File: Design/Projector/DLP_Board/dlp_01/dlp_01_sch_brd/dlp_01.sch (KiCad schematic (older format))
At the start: 0 parts

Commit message: Ongoing updates the schematics
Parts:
- added C? (x2): 22u, Capacitors_SMD:C_1206, symbol Device:C
- added J?: Barrel_Jack_MountingPin, Connectors:BARREL_JACK, symbol Connector:Barrel_Jack_MountingPin
- added R?: 0R, Resistors_SMD:R_1206, symbol Device:R
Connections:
- new net: C?.1, J?.1, R?.2
- new net: C?.1, R?.1
- new net GND: C?.2, C?.2, J?.2
- no-connect marks 0 -> 1

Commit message: More updates in the DLP board
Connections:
- no-connect marks 1 -> 5
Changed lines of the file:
@@
 F64 "PDAT_A_[23..0]" I L 7700 4150 50
 F65 "3DR_A" I L 7700 4350 50
-F66 "mSPI_CLK" O L 7700 2650 50
-F67 "mSPI_MOSI" O L 7700 2700 50
-F68 "mSPI_CSZO" O L 7700 2800 50
-F69 "mSPI_MISO" I L 7700 2750 50
-F70 "mI2C_SCL" O L 7700 3650 50
-F71 "mI2C_SDA" B L 7700 3700 50
-F72 "mHOST_IRQ" O L 7700 5650 50
-F73 "CMP_OUT" I L 7700 6900 50
-F74 "LED_SEL_0" O L 7700 7100 50
-F75 "LED_SEL_1" O L 7700 7150 50
-F76 "sSPI_CLK" O L 7700 2950 50
-F77 "sSPI_MOSI" O L 7700 3000 50
-F78 "sSPI_CSZO" O L 7700 3100 50
-F79 "sSPI_MISO" I L 7700 3050 50
-F80 "sHOST_IRQ" O L 7700 5700 50
-F81 "sI2C_SCL" O L 7700 3850 50
-F82 "sI2C_SDA" B L 7700 3900 50
-F83 "PARKZ" I L 7700 5250 50
-F84 "RESETZ" I L 7700 6800 50
+F66 "mHOST_IRQ" O L 7700 5650 50
+F67 "CMP_OUT" I L 7700 6900 50
+F68 "LED_SEL_0" O L 7700 7100 50
+F69 "LED_SEL_1" O L 7700 7150 50
+F70 "sHOST_IRQ" O L 7700 5700 50
+F71 "PARKZ" I L 7700 5250 50
+F72 "RESETZ" I L 7700 6800 50
+F73 "HOST_SCL" I L 7700 3000 50
+F74 "HOST_SDA" I L 7700 3050 50
+F75 "CONTR0_SCL" I L 7700 3200 50
+F76 "CONTR0_SDA" I L 7700 3250 50
+F77 "CONTR1_SCL" I L 7700 3400 50
+F78 "CONTR1_SDA" I L 7700 3450 50
 $EndSheet
 $Sheet
@@
 F0 "application_connectors" 50
 F1 "application_connectors.sch" 50
+F2 "PCLK_B" O R 7050 4550 50
+F3 "VSYNC_B" O R 7050 4650 50
+F4 "HSYNC_B" O R 7050 4700 50
+F5 "DATEN_B" O R 7050 4750 50
+F6 "PDAT_B_[23..0]" O R 7050 4600 50
+F7 "3DR_B" O R 7050 4800 50
+F8 "PCLK_A" O R 7050 4100 50
+F9 "VSYNC_A" O R 7050 4200 50
+F10 "HSYNC_A" O R 7050 4250 50
+F11 "DATEN_A" O R 7050 4300 50
+F12 "PDAT_A_[23..0]" O R 7050 4150 50
+F13 "3DR_A" O R 7050 4350 50
+F14 "PDM_CVS_TE_B" I R 7050 4850 50
+F15 "PDM_CVS_TE_A" I R 7050 4400 50
+F16 "HOST_SCL" O R 7050 3000 50
+F17 "HOST_SDA" B R 7050 3050 50
+F18 "CONTR0_SCL" O R 7050 3200 50
+F19 "CONTR0_SDA" B R 7050 3250 50
+F20 "CONTR1_SDA" B R 7050 3450 50
+F21 "CONTR1_SCL" O R 7050 3400 50
+F22 "PS_SCL" O R 7050 2600 50
+F23 "PL_SCL" O R 7050 2650 50
+F24 "PL_SDA" B R 7050 2800 50
+F25 "PS_SDA" B R 7050 2850 50
 $EndSheet
 Wire Wire Line
@@
 Wire Wire Line
 	7050 7750 10150 7750
+Wire Wire Line
+	7050 4100 7700 4100
+Wire Wire Line
+	7050 4200 7700 4200
+Wire Bus Line
+	7050 4150 7700 4150
+Wire Wire Line
+	7050 4250 7700 4250
+Wire Wire Line
+	7050 4300 7700 4300
+Wire Wire Line
+	7050 4350 7700 4350
+Wire Wire Line
+	7050 4400 7700 4400
+Wire Wire Line
+	7050 4550 7700 4550
+Wire Bus Line
+	7050 4600 7700 4600
+Wire Wire Line
+	7050 4650 7700 4650
+Wire Wire Line
+	7050 4700 7700 4700
+Wire Wire Line
+	7050 4750 7700 4750
+Wire Wire Line
+	7050 4800 7700 4800
+Wire Wire Line
+	7050 4850 7700 4850
+NoConn ~ 7050 2600
+NoConn ~ 7050 2650
+NoConn ~ 7050 2800
+NoConn ~ 7050 2850
+Wire Wire Line
+	7050 3000 7700 3000
+Wire Wire Line
+	7700 3050 7050 3050
+Wire Wire Line
+	7050 3200 7700 3200
+Wire Wire Line
+	7700 3250 7050 3250
+Wire Wire Line
+	7050 3400 7700 3400
+Wire Wire Line
+	7700 3450 7050 3450
 $EndSCHEMATC

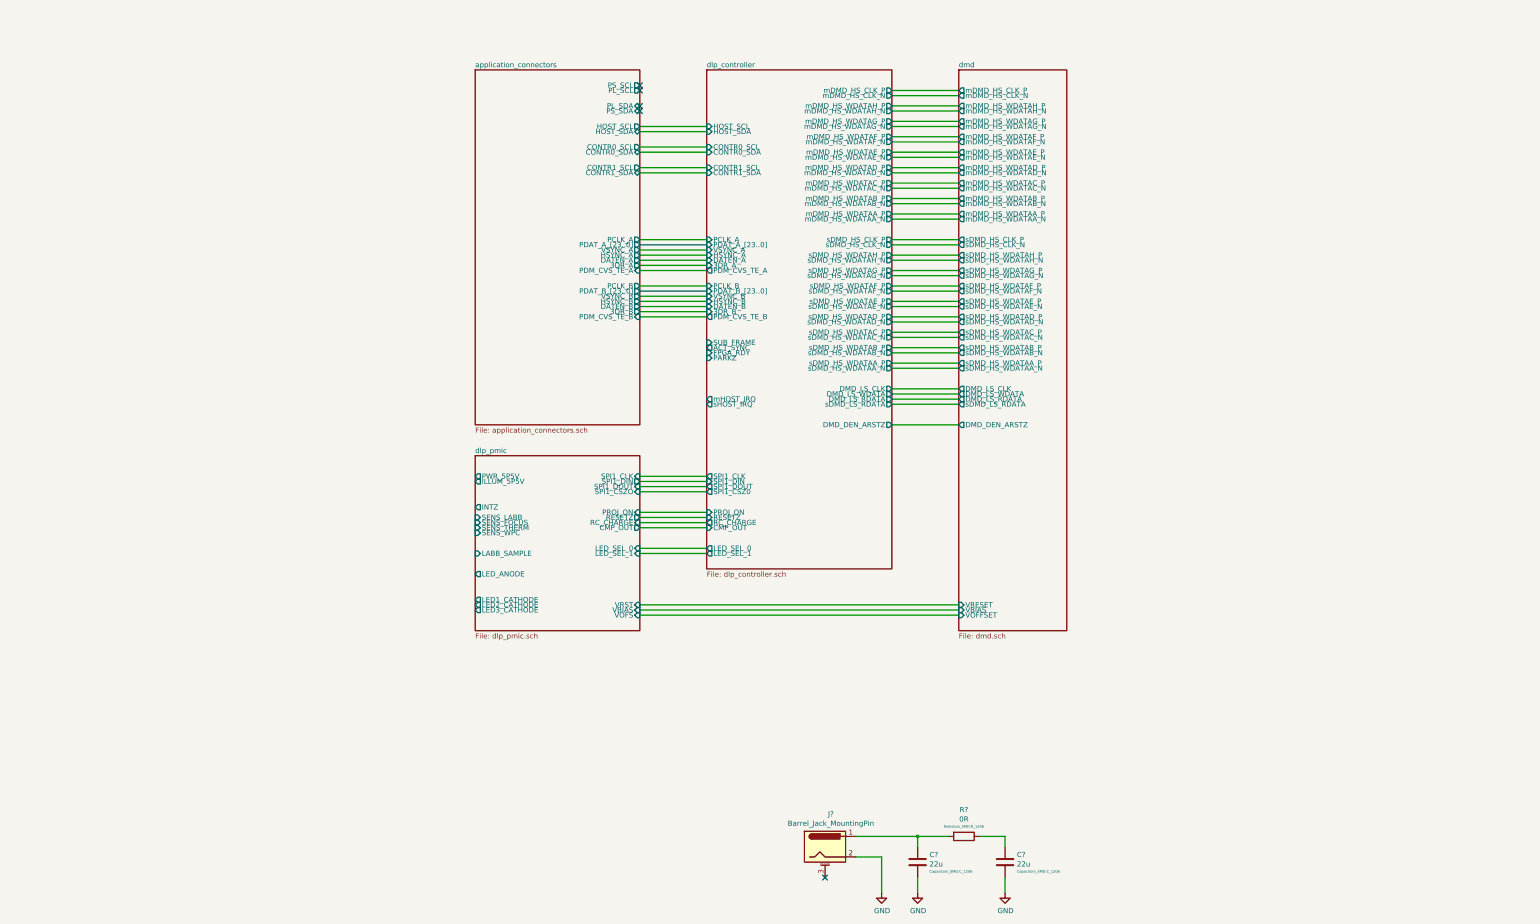
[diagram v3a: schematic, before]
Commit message: Initial placement of power converters, BGA fanout and Z-turn board outline imported
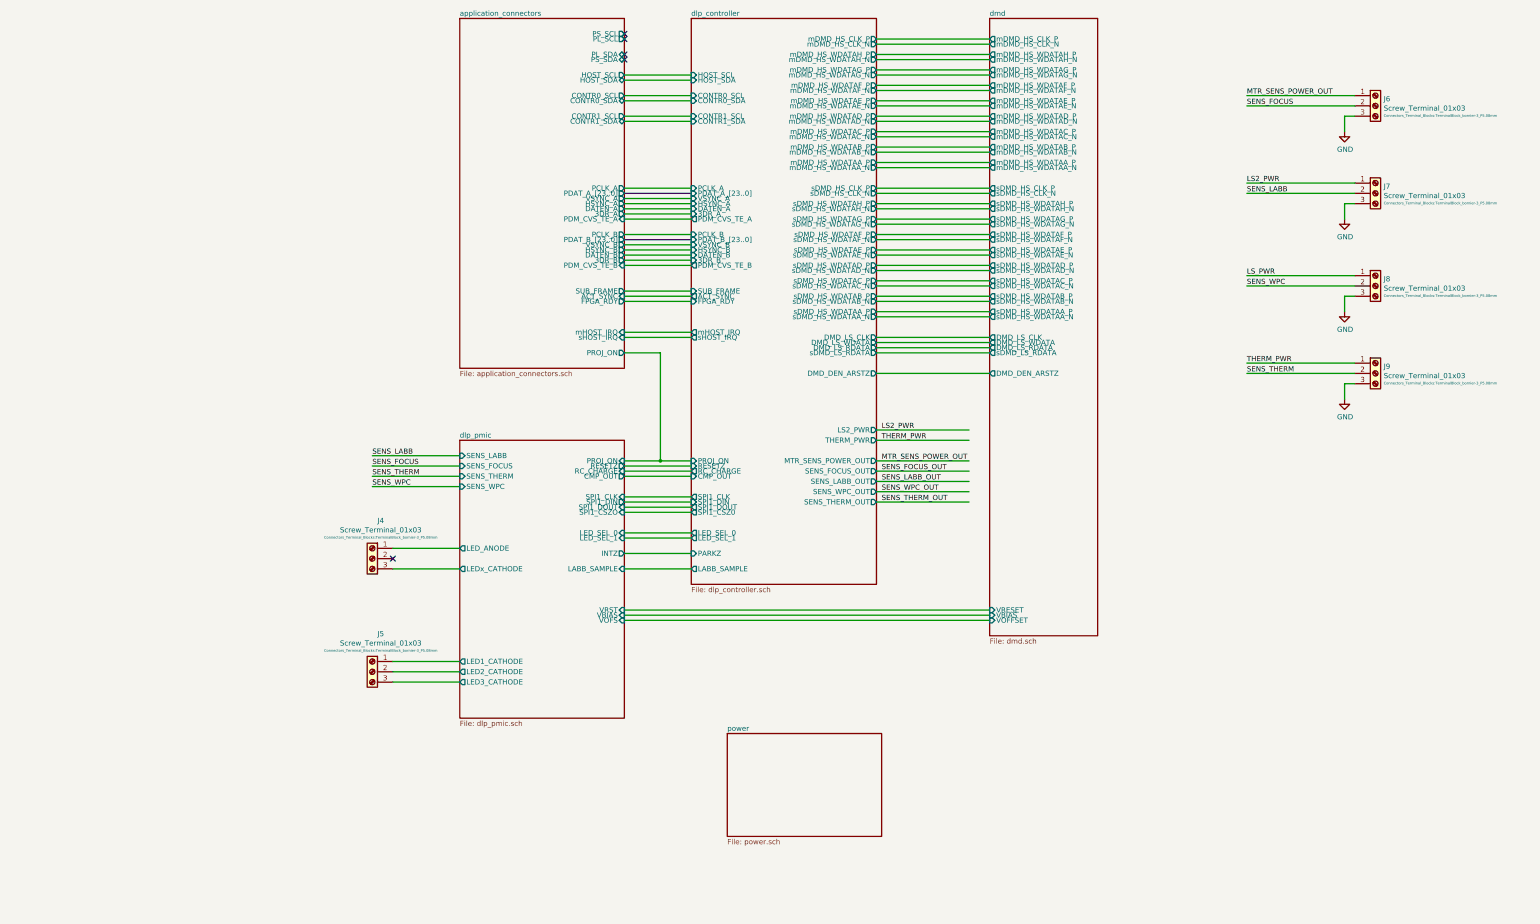
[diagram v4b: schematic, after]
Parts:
- removed C? (x2): 22u, Capacitors_SMD:C_1206, symbol Device:C
- removed J?: Barrel_Jack_MountingPin, Connectors:BARREL_JACK, symbol Connector:Barrel_Jack_MountingPin
- removed R?: 0R, Resistors_SMD:R_1206, symbol Device:R
- added J4, J5, J6, J7, J8, J9: Screw_Terminal_01x03, Connectors_Terminal_Blocks:TerminalBlock_bornier-3_P5.08mm, symbol Connector:Screw_Terminal_01x03
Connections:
- net labels added: LS2_PWR, LS_PWR, MTR_SENS_POWER_OUT, SENS_FOCUS, SENS_FOCUS_OUT, SENS_LABB, SENS_LABB_OUT, SENS_THERM, SENS_THERM_OUT, SENS_WPC, SENS_WPC_OUT, THERM_PWR
- wire segments 81 -> 114

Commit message: Initial component placement on PCB
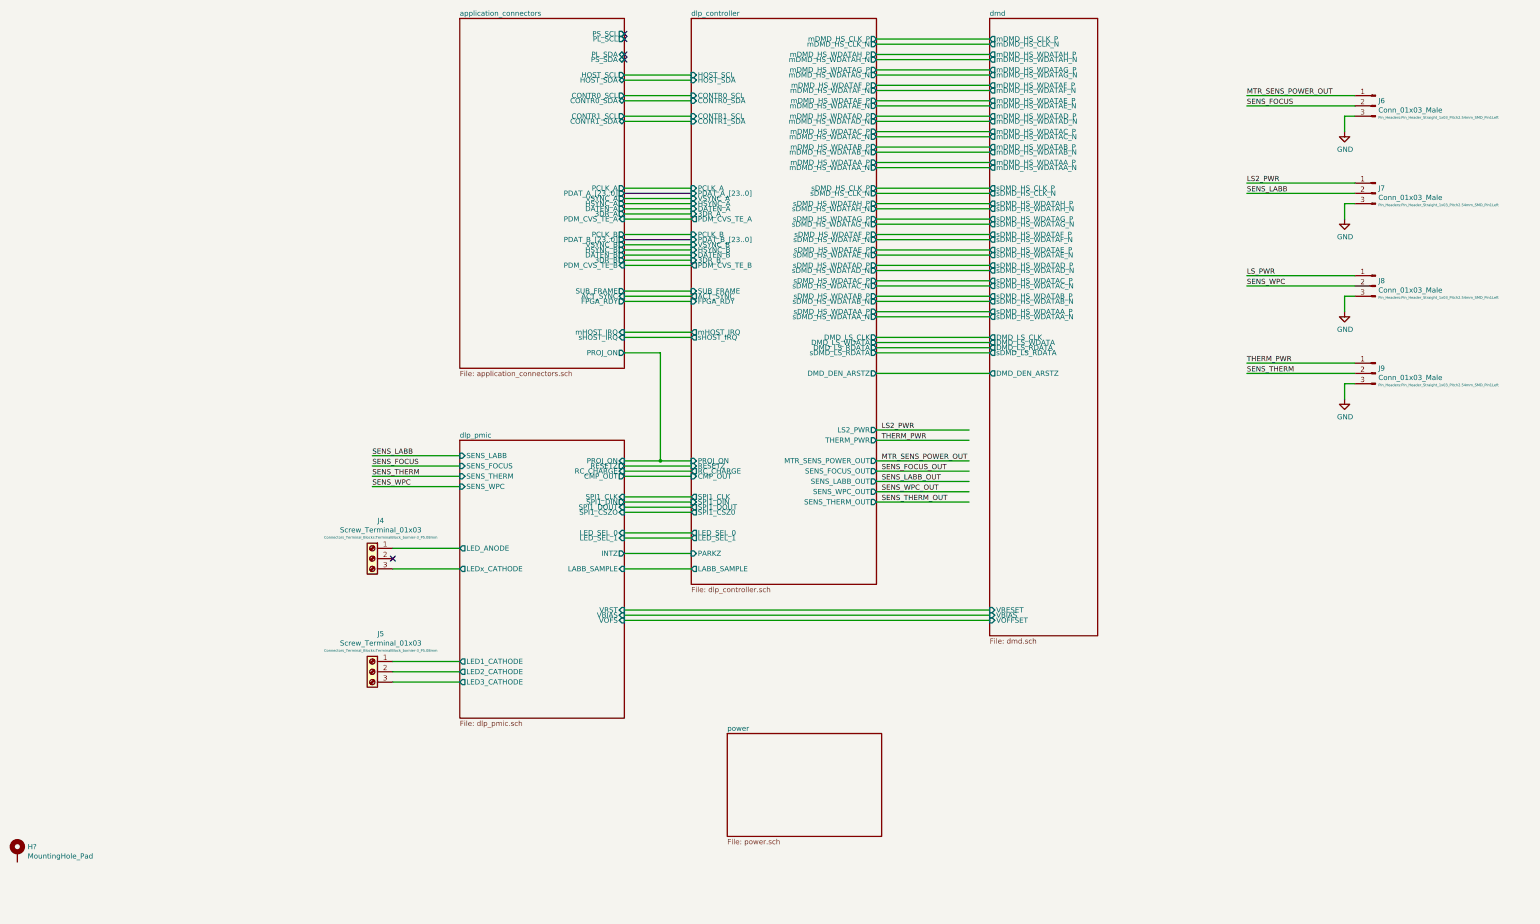
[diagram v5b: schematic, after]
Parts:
- removed J6, J7, J8, J9: Screw_Terminal_01x03, Connectors_Terminal_Blocks:TerminalBlock_bornier-3_P5.08mm, symbol Connector:Screw_Terminal_01x03
- added H?: MountingHole_Pad, symbol Mechanical:MountingHole_Pad
- added J6, J7, J8, J9: Conn_01x03_Male, Pin_Headers:Pin_Header_Straight_1x03_Pitch2.54mm_SMD_Pin1Left, symbol Connector:Conn_01x03_Male
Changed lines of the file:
@@
 	10250 6650 9350 6650
-$Comp
-L Connector:Screw_Terminal_01x03 J6
-U 1 1 5DBFE081
-P 14200 2800
-F 0 "J6" H 14280 2868 50  0000 L CNN
-F 1 "Screw_Terminal_01x03" H 14280 2777 50  0000 L CNN
-F 2 "Connectors_Terminal_Blocks:TerminalBlock_bornier-3_P5.08mm" H 14280 2705 25  0000 L CNN
-F 3 "~" H 14200 2800 50  0001 C CNN
-	1    14200 2800
-	1    0    0    -1
-$EndComp
 $Comp
 L power:GND #PWR0121
@@
 SENS_FOCUS
 $Comp
-L Connector:Screw_Terminal_01x03 J7
-U 1 1 5DC4AEBF
-P 14200 3650
-F 0 "J7" H 14280 3718 50  0000 L CNN
-F 1 "Screw_Terminal_01x03" H 14280 3627 50  0000 L CNN
-F 2 "Connectors_Terminal_Blocks:TerminalBlock_bornier-3_P5.08mm" H 14280 3555 25  0000 L CNN
-F 3 "~" H 14200 3650 50  0001 C CNN
-	1    14200 3650
-	1    0    0    -1
-$EndComp
-$Comp
 L power:GND #PWR0122
 U 1 1 5DC4AEC9
@@
 SENS_LABB
 $Comp
-L Connector:Screw_Terminal_01x03 J8
-U 1 1 5DC57EB3
-P 14200 4550
-F 0 "J8" H 14280 4618 50  0000 L CNN
-F 1 "Screw_Terminal_01x03" H 14280 4527 50  0000 L CNN
-F 2 "Connectors_Terminal_Blocks:TerminalBlock_bornier-3_P5.08mm" H 14280 4455 25  0000 L CNN
-F 3 "~" H 14200 4550 50  0001 C CNN
-	1    14200 4550
-	1    0    0    -1
-$EndComp
-$Comp
 L power:GND #PWR0123
 U 1 1 5DC57EBD
@@
 Text Label 12950 4550 0    50   ~ 0
 SENS_WPC
-$Comp
-L Connector:Screw_Terminal_01x03 J9
-U 1 1 5DC57ECD
-P 14200 5400
-F 0 "J9" H 14280 5468 50  0000 L CNN
-F 1 "Screw_Terminal_01x03" H 14280 5377 50  0000 L CNN
-F 2 "Connectors_Terminal_Blocks:TerminalBlock_bornier-3_P5.08mm" H 14280 5305 25  0000 L CNN
-F 3 "~" H 14200 5400 50  0001 C CNN
-	1    14200 5400
-	1    0    0    -1
-$EndComp
 $Comp
 L power:GND #PWR0124
@@
 	4650 8400 5300 8400
 NoConn ~ 4650 7200
+$Comp
+L Connector:Conn_01x03_Male J6
+U 1 1 5D6C113E
+P 14200 2800
+F 0 "J6" H 14172 2850 50  0000 R CNN
+F 1 "Conn_01x03_Male" H 14172 2759 50  0000 R CNN
+F 2 "Pin_Headers:Pin_Header_Straight_1x03_Pitch2.54mm_SMD_Pin1Left" H 14172 2687 25  0000 R CNN
+F 3 "~" H 14200 2800 50  0001 C CNN
+	1    14200 2800
+	-1   0    0    -1
+$EndComp
+$Comp
+L Connector:Conn_01x03_Male J7
+U 1 1 5D6D14C7
+P 14200 3650
+F 0 "J7" H 14172 3700 50  0000 R CNN
+F 1 "Conn_01x03_Male" H 14172 3609 50  0000 R CNN
+F 2 "Pin_Headers:Pin_Header_Straight_1x03_Pitch2.54mm_SMD_Pin1Left" H 14172 3537 25  0000 R CNN
+F 3 "~" H 14200 3650 50  0001 C CNN
+	1    14200 3650
+	-1   0    0    -1
+$EndComp
+$Comp
+L Connector:Conn_01x03_Male J8
+U 1 1 5D6D7EFB
+P 14200 4550
+F 0 "J8" H 14172 4600 50  0000 R CNN
+F 1 "Conn_01x03_Male" H 14172 4509 50  0000 R CNN
+F 2 "Pin_Headers:Pin_Header_Straight_1x03_Pitch2.54mm_SMD_Pin1Left" H 14172 4437 25  0000 R CNN
+F 3 "~" H 14200 4550 50  0001 C CNN
+	1    14200 4550
+	-1   0    0    -1
+$EndComp
+$Comp
+L Connector:Conn_01x03_Male J9
+U 1 1 5D6DEB5D
+P 14200 5400
+F 0 "J9" H 14172 5450 50  0000 R CNN
+F 1 "Conn_01x03_Male" H 14172 5359 50  0000 R CNN
+F 2 "Pin_Headers:Pin_Header_Straight_1x03_Pitch2.54mm_SMD_Pin1Left" H 14172 5287 25  0000 R CNN
+F 3 "~" H 14200 5400 50  0001 C CNN
+	1    14200 5400
+	-1   0    0    -1
+$EndComp
+$Comp
+L Mechanical:MountingHole_Pad H?
+U 1 1 5D747231
+P 1000 10050
+F 0 "H?" H 1100 10099 50  0000 L CNN
+F 1 "MountingHole_Pad" H 1100 10008 50  0000 L CNN
+F 2 "" H 1000 10050 50  0001 C CNN
+F 3 "~" H 1000 10050 50  0001 C CNN
+	1    1000 10050
+	1    0    0    -1
+$EndComp
 $EndSCHEMATC

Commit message: Schematic and PCB complete ready for review
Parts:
- added H2, H3, H4, H5, H6: 3mm, Mounting_Holes:MountingHole_3mm_Pad_Via, symbol Mechanical:MountingHole_Pad
- H1: renamed from H?; value MountingHole_Pad -> 3mm; footprint (none) -> Mounting_Holes:MountingHole_3mm_Pad_Via
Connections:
- wire segments 114 -> 126
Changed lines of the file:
@@
 $EndComp
 $Comp
-L Mechanical:MountingHole_Pad H?
+L Mechanical:MountingHole_Pad H1
 U 1 1 5D747231
 P 1000 10050
-F 0 "H?" H 1100 10099 50  0000 L CNN
-F 1 "MountingHole_Pad" H 1100 10008 50  0000 L CNN
-F 2 "" H 1000 10050 50  0001 C CNN
+F 0 "H1" H 1100 10099 50  0000 L CNN
+F 1 "3mm" H 1100 10008 50  0000 L CNN
+F 2 "Mounting_Holes:MountingHole_3mm_Pad_Via" H 1000 10050 50  0001 C CNN
 F 3 "~" H 1000 10050 50  0001 C CNN
 	1    1000 10050
 	1    0    0    -1
 $EndComp
+$Comp
+L Mechanical:MountingHole_Pad H2
+U 1 1 5D8ACB34
+P 1400 10050
+F 0 "H2" H 1500 10099 50  0000 L CNN
+F 1 "3mm" H 1500 10008 50  0000 L CNN
+F 2 "Mounting_Holes:MountingHole_3mm_Pad_Via" H 1400 10050 50  0001 C CNN
+F 3 "~" H 1400 10050 50  0001 C CNN
+	1    1400 10050
+	1    0    0    -1
+$EndComp
+$Comp
+L Mechanical:MountingHole_Pad H3
+U 1 1 5D8ACE3C
+P 1800 10050
+F 0 "H3" H 1900 10099 50  0000 L CNN
+F 1 "3mm" H 1900 10008 50  0000 L CNN
+F 2 "Mounting_Holes:MountingHole_3mm_Pad_Via" H 1800 10050 50  0001 C CNN
+F 3 "~" H 1800 10050 50  0001 C CNN
+	1    1800 10050
+	1    0    0    -1
+$EndComp
+$Comp
+L Mechanical:MountingHole_Pad H4
+U 1 1 5D8AD183
+P 2200 10050
+F 0 "H4" H 2300 10099 50  0000 L CNN
+F 1 "3mm" H 2300 10008 50  0000 L CNN
+F 2 "Mounting_Holes:MountingHole_3mm_Pad_Via" H 2200 10050 50  0001 C CNN
+F 3 "~" H 2200 10050 50  0001 C CNN
+	1    2200 10050
+	1    0    0    -1
+$EndComp
+$Comp
+L power:GND #PWR0141
+U 1 1 5D8ADFB2
+P 1000 10450
+F 0 "#PWR0141" H 1000 10200 50  0001 C CNN
+F 1 "GND" H 1005 10277 50  0000 C CNN
+F 2 "" H 1000 10450 50  0001 C CNN
+F 3 "" H 1000 10450 50  0001 C CNN
+	1    1000 10450
+	1    0    0    -1
+$EndComp
+Wire Wire Line
+	1000 10150 1000 10300
+Wire Wire Line
+	2200 10150 2200 10300
+Wire Wire Line
+	2200 10300 1800 10300
+Connection ~ 1000 10300
+Wire Wire Line
+	1000 10300 1000 10450
+Wire Wire Line
+	1400 10150 1400 10300
+Connection ~ 1400 10300
+Wire Wire Line
+	1400 10300 1000 10300
+Wire Wire Line
+	1800 10150 1800 10300
+Connection ~ 1800 10300
+Wire Wire Line
+	1800 10300 1400 10300
+$Comp
+L Mechanical:MountingHole_Pad H5
+U 1 1 5D8D612D
+P 2600 10050
+F 0 "H5" H 2700 10099 50  0000 L CNN
+F 1 "3mm" H 2700 10008 50  0000 L CNN
+F 2 "Mounting_Holes:MountingHole_3mm_Pad_Via" H 2600 10050 50  0001 C CNN
+F 3 "~" H 2600 10050 50  0001 C CNN
+	1    2600 10050
+	1    0    0    -1
+$EndComp
+$Comp
+L Mechanical:MountingHole_Pad H6
+U 1 1 5D8D6133
+P 3000 10050
+F 0 "H6" H 3100 10099 50  0000 L CNN
+F 1 "3mm" H 3100 10008 50  0000 L CNN
+F 2 "Mounting_Holes:MountingHole_3mm_Pad_Via" H 3000 10050 50  0001 C CNN
+F 3 "~" H 3000 10050 50  0001 C CNN
+	1    3000 10050
+	1    0    0    -1
+$EndComp
+Wire Wire Line
+	3000 10150 3000 10300
+Wire Wire Line
+	3000 10300 2600 10300
+Wire Wire Line
+	2600 10150 2600 10300
+Connection ~ 2600 10300
+Wire Wire Line
+	2600 10300 2200 10300
+Connection ~ 2200 10300
 $EndSCHEMATC
